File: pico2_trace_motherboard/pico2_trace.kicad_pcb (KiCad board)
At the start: 2 copper layers, 65 x 34 mm, 0 parts

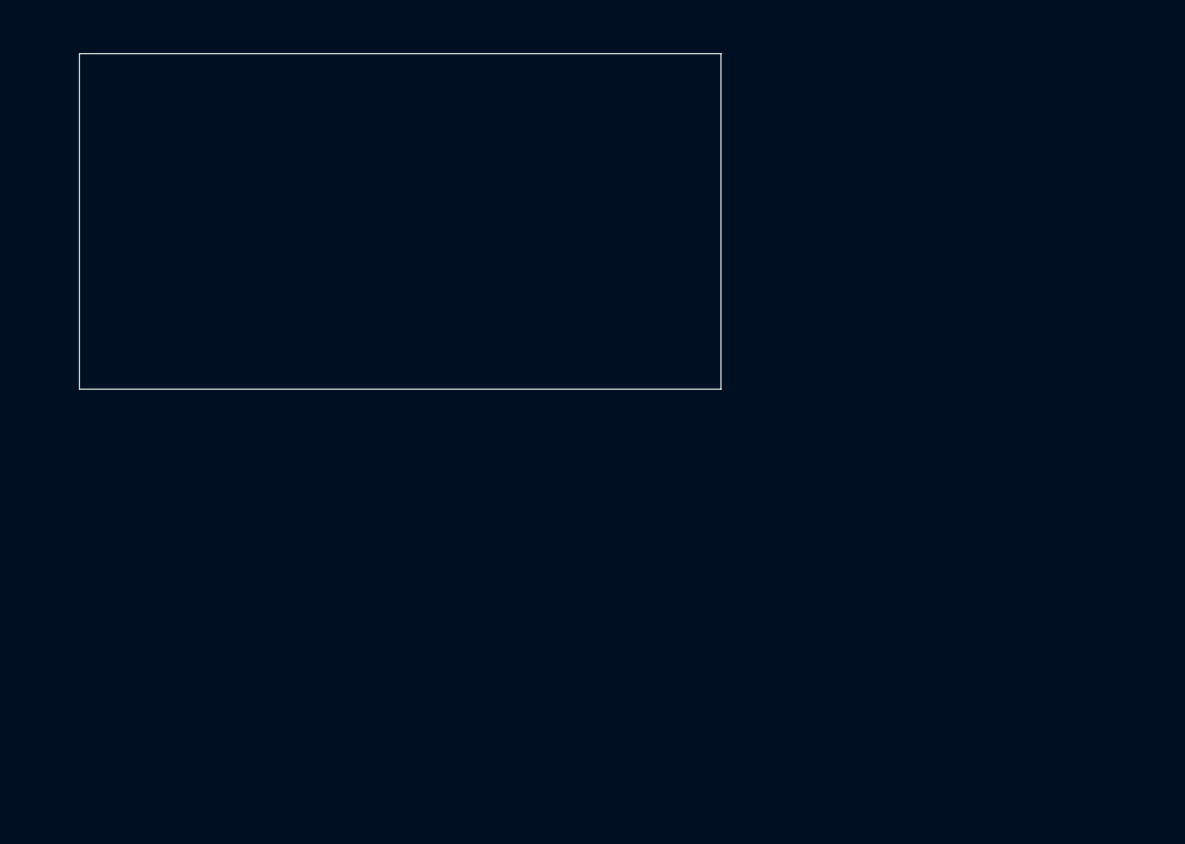
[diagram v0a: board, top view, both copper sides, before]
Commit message: pcb: footprints, nets, outline, constrained placement + trace silk
Squash of cd813c2, 6b1452c, 6e620d1.
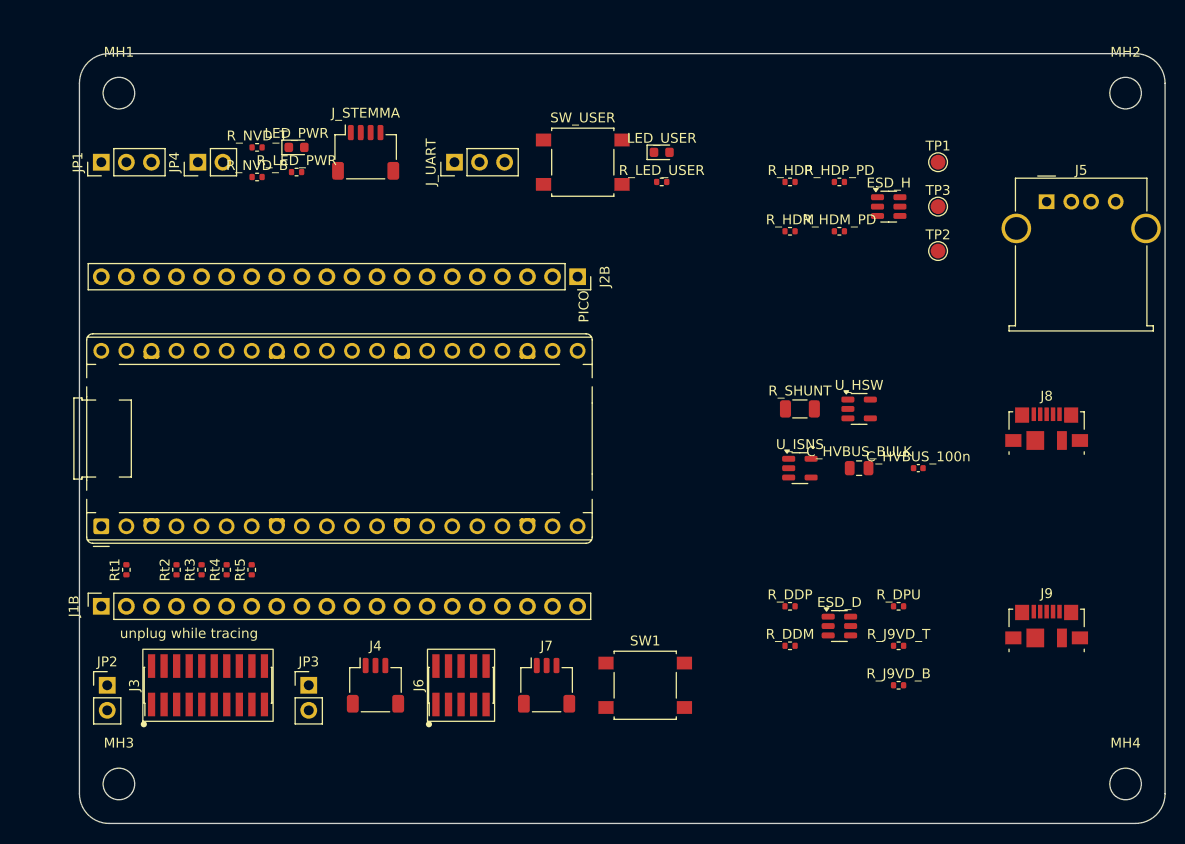
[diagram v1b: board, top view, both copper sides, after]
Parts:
- added C_HVBUS_100n: 100n, C_0402_1005Metric, F.Cu at (85.0, 42.0)
- added C_HVBUS_BULK: 22u, C_0805_2012Metric, F.Cu at (79.0, 42.0)
- added ESD_D: USBLC6-2SC6, SOT-23-6, F.Cu at (77.0, 58.0)
- added ESD_H: USBLC6-2SC6, SOT-23-6, F.Cu at (82.0, 15.5)
- added J1B: BREAKOUT, PinSocket_1x20_P2.54mm_Vertical, F.Cu at (2.21, 56.0)
- added J2B: BREAKOUT, PinSocket_1x20_P2.54mm_Vertical, F.Cu at (50.5, 22.6)
- added J3: MIPI-20, FTSH-110-01-DV, F.Cu at (13.0, 64.0)
- added J4: JST-SH-3 DEBUG, JST_SH_SM03B-SRSS-TB_1x03-1MP_P1.00mm_Horizontal, F.Cu at (30.0, 64.0)
- added J5: USB-A HOST, USB_A_Molex_67643_Horizontal, F.Cu at (98.0, 15.0)
- added J6: CORTEX-10, FTSH-105-01-DV, F.Cu at (38.7, 64.0)
- added J7: JST-SH-3 DEBUG_PROBE, JST_SH_SM03B-SRSS-TB_1x03-1MP_P1.00mm_Horizontal, F.Cu at (47.3, 64.0)
- added J8: USB-MICROB PWR, USB_Micro-B_Molex_47346-0001, F.Cu at (98.0, 38.0)
- added J9: USB-MICROB DEV, USB_Micro-B_Molex_47346-0001, F.Cu at (98.0, 58.0)
- added JP1: 5V SEL, PinHeader_1x03_P2.54mm_Vertical, F.Cu at (2.21, 11.0)
- added JP2: GP0 GUARD, PinHeader_1x02_P2.54mm_Vertical, F.Cu at (2.81, 64.0)
- added JP3: GP6 GUARD, PinHeader_1x02_P2.54mm_Vertical, F.Cu at (23.2, 64.0)
- added JP4: VBUS_DET EN, PinHeader_1x02_P2.54mm_Vertical, F.Cu at (12.0, 11.0)
- added J_STEMMA: STEMMA-QT, JST_SH_SM04B-SRSS-TB_1x04-1MP_P1.00mm_Horizontal, F.Cu at (29.0, 10.0)
- added J_UART: UART0, PinHeader_1x03_P2.54mm_Vertical, F.Cu at (38.0, 11.0)
- added LED_PWR: LED, LED_0603_1608Metric, F.Cu at (22.0, 9.50)
- added LED_USER: LED, LED_0603_1608Metric, F.Cu at (59.0, 10.0)
- added MH1: MountingHole_3.2mm_M3, MountingHole_3.2mm_M3, F.Cu at (4.00, 4.00)
- added MH2: MountingHole_3.2mm_M3, MountingHole_3.2mm_M3, F.Cu at (106.0, 4.00)
- added MH3: MountingHole_3.2mm_M3, MountingHole_3.2mm_M3, F.Cu at (4.00, 74.0)
- added MH4: MountingHole_3.2mm_M3, MountingHole_3.2mm_M3, F.Cu at (106.0, 74.0)
- added PICO: Pico2, RaspberryPi_Pico_Common_THT, F.Cu at (2.21, 47.9)
- added R_DDM: 22, R_0402_1005Metric, F.Cu at (72.0, 60.0)
- added R_DDP: 22, R_0402_1005Metric, F.Cu at (72.0, 56.0)
- added R_DPU: 1.5k, R_0402_1005Metric, F.Cu at (83.0, 56.0)
- added R_HDM: 22, R_0402_1005Metric, F.Cu at (72.0, 18.0)
- added R_HDM_PD: 15k, R_0402_1005Metric, F.Cu at (77.0, 18.0)
- added R_HDP: 22, R_0402_1005Metric, F.Cu at (72.0, 13.0)
- added R_HDP_PD: 15k, R_0402_1005Metric, F.Cu at (77.0, 13.0)
- added R_J9VD_B: 8.2k, R_0402_1005Metric, F.Cu at (83.0, 64.0)
- added R_J9VD_T: 8.2k, R_0402_1005Metric, F.Cu at (83.0, 60.0)
- added R_LED_PWR: 1k, R_0402_1005Metric, F.Cu at (22.0, 12.0)
- added R_LED_USER: 1k, R_0402_1005Metric, F.Cu at (59.0, 13.0)
- added R_NVD_B: 8.2k, R_0402_1005Metric, F.Cu at (18.0, 12.5)
- added R_NVD_T: 8.2k, R_0402_1005Metric, F.Cu at (18.0, 9.50)
- added R_SHUNT: 0.1, R_1206_3216Metric, F.Cu at (73.0, 36.0)
- added Rt1: 27, R_0402_1005Metric, F.Cu at (4.75, 52.3)
- added Rt2: 27, R_0402_1005Metric, F.Cu at (9.84, 52.3)
- added Rt3: 27, R_0402_1005Metric, F.Cu at (12.4, 52.3)
- added Rt4: 27, R_0402_1005Metric, F.Cu at (14.9, 52.3)
- added Rt5: 27, R_0402_1005Metric, F.Cu at (17.5, 52.3)
- added SW1: RESET, SW_SPST_B3S-1000, F.Cu at (57.3, 64.0)
- added SW_USER: USER, SW_SPST_B3S-1000, F.Cu at (51.0, 11.0)
- added TP1: TP, TestPoint_Pad_D1.5mm, F.Cu at (87.0, 11.0)
- added TP2: TP, TestPoint_Pad_D1.5mm, F.Cu at (87.0, 20.0)
- added TP3: TP, TestPoint_Pad_D1.5mm, F.Cu at (87.0, 15.5)
- added U_HSW: TPS2051B, SOT-23-5, F.Cu at (79.0, 36.0)
- added U_ISNS: INA180A1DBVR, SOT-23-5, F.Cu at (73.0, 42.0)
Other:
- board size 65 x 34 mm -> 110 x 78 mm
- board text added: "unplug while tracing"

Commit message: pcb: trace bundle, SWD tree, power/USB routing; DNP realization
Length-matched trace bundle; edge connectors rotated to face edges;
INA219 option, EN pulldown, cap ratings. Squash of 5ebbf61..2de5eea (4).
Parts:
- added C_NRESET: 100n/16V, C_0402_1005Metric, F.Cu at (0.00, 0.00)
- added D_J9_BUSPWR: 1N4148W, D_SOD-123, F.Cu at (0.00, 0.00)
- added J_TRACE_TP: TRACE_TP, PinHeader_1x06_P2.54mm_Vertical, F.Cu at (0.00, 0.00)
- added R_HVEN_PD: 100k, R_0402_1005Metric, F.Cu at (0.00, 0.00)
- added U_INA219_ALT: INA219, SOT-23-8, F.Cu at (0.00, 0.00)
- C_HVBUS_100n: value 100n -> 100n/16V
- C_HVBUS_BULK: value 22u -> 22u/10V
- moved ESD_D 9.17 mm to (85.3, 62.0)
- moved J8 9.17 mm to (106.3, 42.0), turned to 90 degrees
- moved J9 9.17 mm to (106.3, 62.0), turned to 90 degrees
- moved R_DDM 9.17 mm to (80.3, 64.0)
- moved R_DDP 9.17 mm to (80.3, 60.0)
- moved R_DPU 9.17 mm to (91.3, 60.0)
- moved R_J9VD_B 9.17 mm to (91.3, 68.0)
- moved R_J9VD_T 9.17 mm to (91.3, 64.0)
- moved ESD_H 6.65 mm to (80.6, 22.0)
- moved J5 6.65 mm to (96.6, 21.5), turned to 90 degrees
- moved R_HDM 6.65 mm to (70.6, 24.5)
- moved R_HDM_PD 6.65 mm to (75.6, 24.5)
- moved R_HDP 6.65 mm to (70.6, 19.5)
- moved R_HDP_PD 6.65 mm to (75.6, 19.5)
- moved TP1 6.65 mm to (85.6, 17.5)
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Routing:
- net VBUS_NET: track 0.00 -> 171.2 mm, vias 0 -> 2
- net P3V3: track 0.00 -> 129.8 mm, vias 0 -> 8
- net NRESET: track 0.00 -> 124.8 mm, vias 0 -> 9
- net VBUS_SEL: track 0.00 -> 108.3 mm, vias 0 -> 2
- net SWDIO: track 0.00 -> 71.7 mm, vias 0 -> 4
- net SWCLK: track 0.00 -> 69.2 mm, vias 0 -> 12
- net NATIVE_VBUS_DET: track 0.00 -> 61.3 mm
- net HOST_VBUS: track 0.00 -> 48.0 mm, vias 0 -> 2
- net HOST_DM: track 0.00 -> 30.7 mm
- net DEV_DP: track 0.00 -> 28.8 mm
- net HOST_DP: track 0.00 -> 28.4 mm
- net J9_VBUS: track 0.00 -> 21.1 mm
- net HOST_5V_IN: track 0.00 -> 20.4 mm
- net TD1: track 0.00 -> 19.6 mm
- net TD2: track 0.00 -> 19.2 mm
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
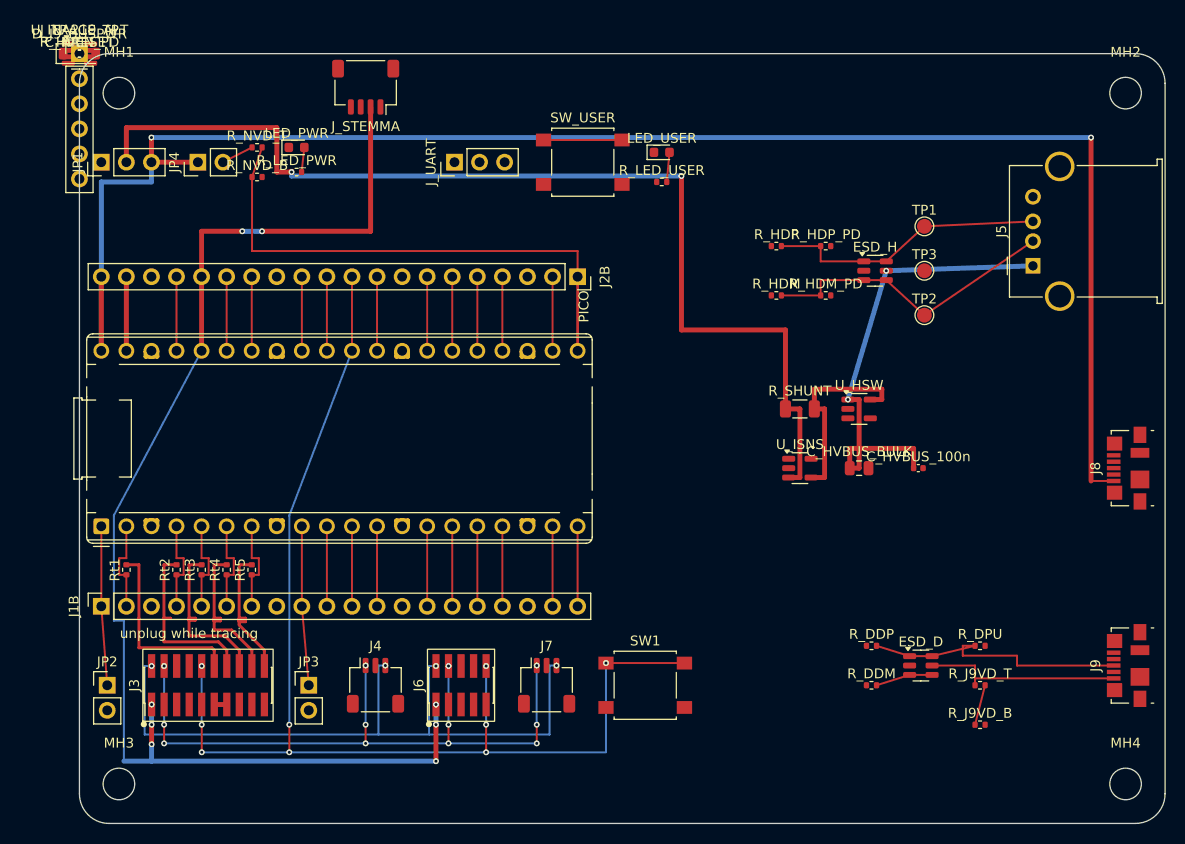
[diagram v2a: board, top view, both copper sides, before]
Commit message: pcb: compact to 92x64; SMT-socket detour reverted to THT
Co-designed placement + routing rewrite; hand-inserted connectors back
to THT after the SMD experiment. Squash of 4fb3f47..d5493a2 (5).
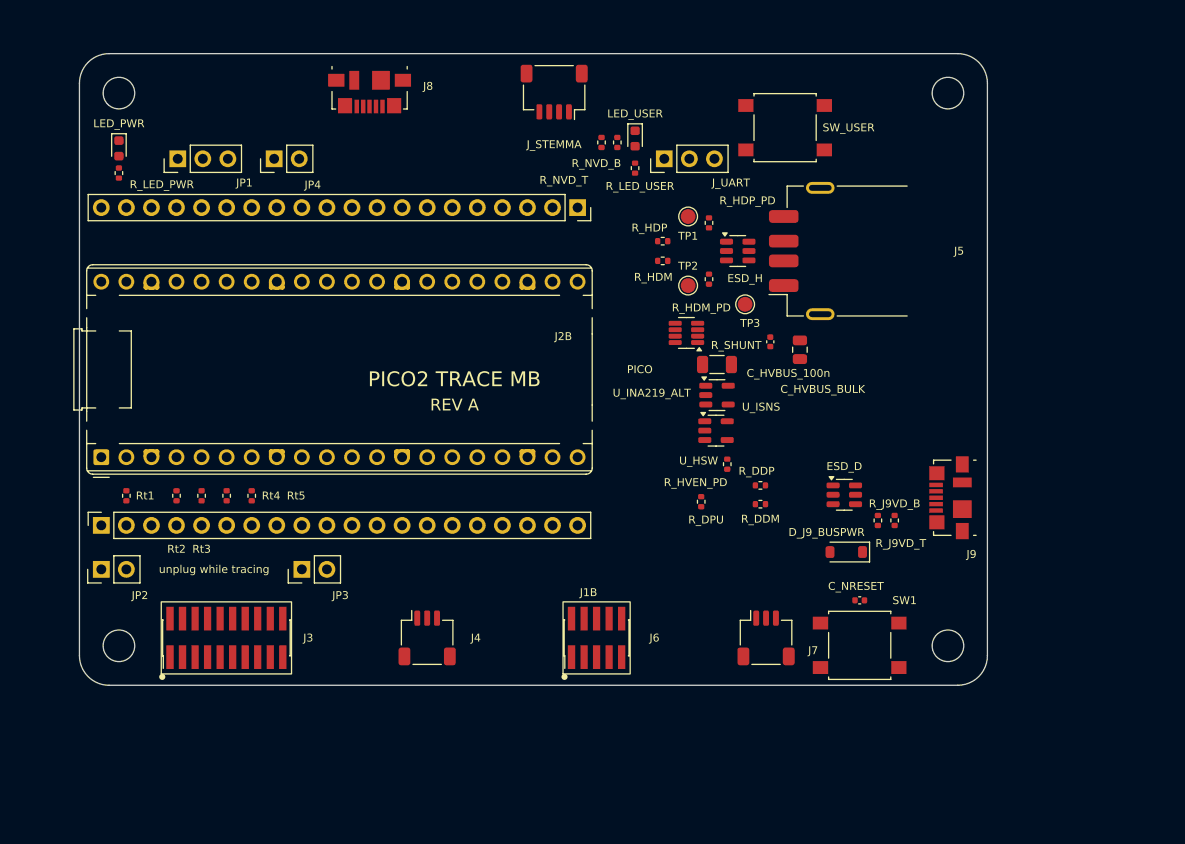
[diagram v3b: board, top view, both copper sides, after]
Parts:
- removed J_TRACE_TP: TRACE_TP, PinHeader_1x06_P2.54mm_Vertical
- J5: footprint USB_A_Molex_67643_Horizontal -> USB_A_Receptacle_GCT_USB1046
- moved C_NRESET 96.5 mm to (79.1, 55.4)
- moved D_J9_BUSPWR 92.7 mm to (77.7, 50.5), turned to 180 degrees
- moved J8 85.8 mm to (29.4, 3.90), turned to 180 degrees
- moved R_HVEN_PD 77.7 mm to (65.6, 41.6), turned to -90 degrees
- moved U_INA219_ALT 67.7 mm to (61.5, 28.3), turned to 180 degrees
- moved R_NVD_B 36.7 mm to (54.5, 9.00), turned to -90 degrees
- moved R_NVD_T 34.9 mm to (52.9, 9.00), turned to 90 degrees
- moved R_DPU 31.8 mm to (63.0, 45.4), turned to -90 degrees
- moved J9 24.8 mm to (88.3, 45.0)
- moved TP2 24.1 mm to (61.7, 23.5)
- moved TP1 24.0 mm to (61.7, 16.5)
- moved R_J9VD_B 23.1 mm to (80.9, 47.3), turned to -90 degrees
- moved MH4 22.8 mm to (88.0, 60.0)
- moved J7 22.7 mm to (69.6, 59.2)
- moved SW1 22.1 mm to (79.1, 60.0)
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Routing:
- net VBUS_NET: track 171.2 -> 0.00 mm, vias 2 -> 0
- net P3V3: track 129.8 -> 0.00 mm, vias 8 -> 0
- net NRESET: track 124.8 -> 0.00 mm, vias 9 -> 0
- net VBUS_SEL: track 108.3 -> 0.00 mm, vias 2 -> 0
- net SWDIO: track 71.7 -> 0.00 mm, vias 4 -> 0
- net SWCLK: track 69.2 -> 0.00 mm, vias 12 -> 0
- net NATIVE_VBUS_DET: track 61.3 -> 0.00 mm
- net HOST_VBUS: track 48.0 -> 0.00 mm, vias 2 -> 0
- net HOST_DM: track 30.7 -> 0.00 mm
- net DEV_DP: track 28.8 -> 0.00 mm
- net HOST_DP: track 28.4 -> 0.00 mm
- net J9_VBUS: track 21.1 -> 0.00 mm
- net HOST_5V_IN: track 20.4 -> 0.00 mm
- net TD1: track 19.6 -> 0.00 mm
- net TD2: track 19.2 -> 0.00 mm
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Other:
- board size 110 x 78 mm -> 92 x 64 mm
- board text added: "PICO2 TRACE MB"
- board text added: "REV A"

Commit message: pcb: complete routing, GND pours + stitching, power widening
All copper 0 non-GND unconnected; J10 SWD dupont added, redundant J4
removed, antenna keepout cleared; VBUS_NET widened; both-layer GND
zones + stitching vias. Squash of 0dd589d, 7224fb8, 98ee5bf, 9fa26b4.
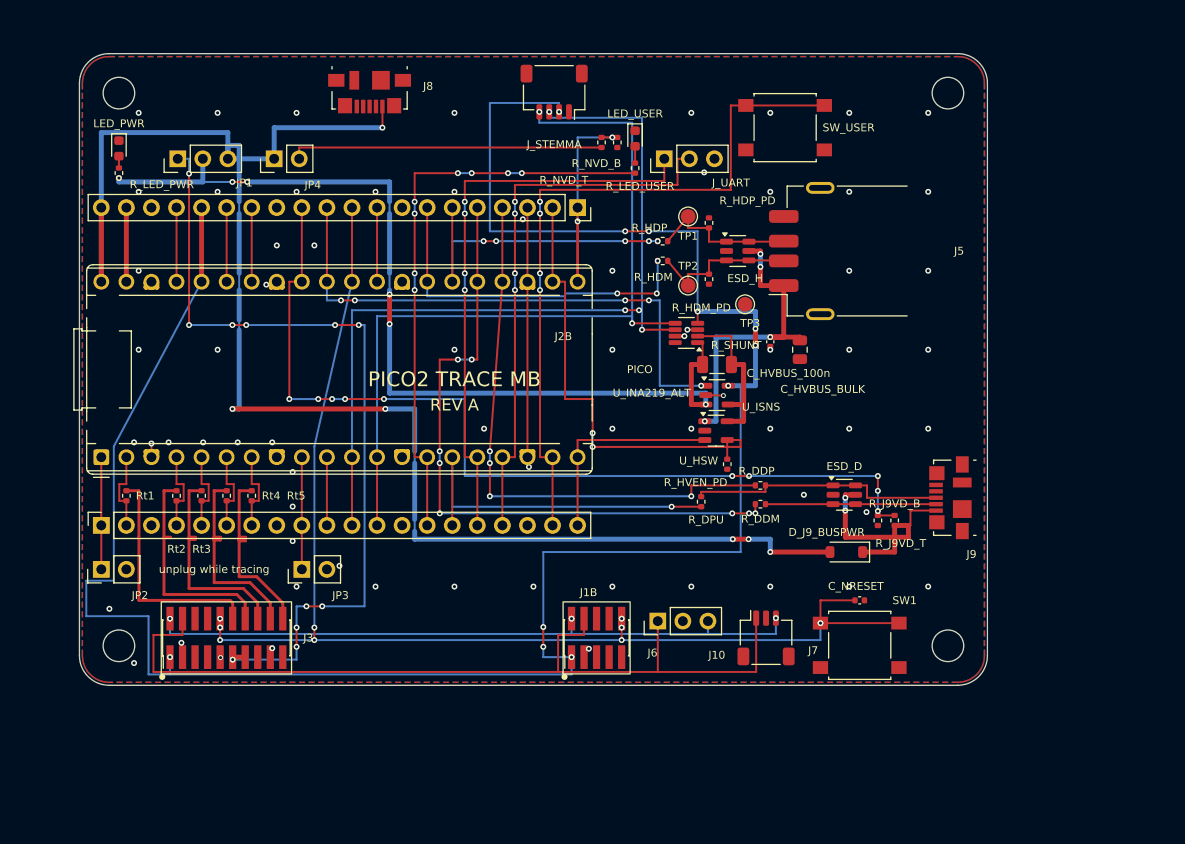
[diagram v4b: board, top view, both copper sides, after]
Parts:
- removed J4: JST-SH-3 DEBUG, JST_SH_SM03B-SRSS-TB_1x03-1MP_P1.00mm_Horizontal
- added J10: SWD, PinHeader_1x03_P2.54mm_Vertical, F.Cu at (58.6, 57.5)
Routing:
- net P3V3: track 0.00 -> 224.0 mm, vias 0 -> 11
- net VBUS_NET: track 0.00 -> 164.0 mm, vias 0 -> 6
- net NRESET: track 0.00 -> 124.9 mm, vias 0 -> 9
- net VBUS_SEL: track 0.00 -> 94.1 mm, vias 0 -> 6
- net DEV_VBUS_DET: track 0.00 -> 93.8 mm, vias 0 -> 10
- net SWCLK: track 0.00 -> 88.0 mm
- net I2C0_SDA: track 0.00 -> 88.0 mm, vias 0 -> 4
- net V5_JTRACE: track 0.00 -> 84.6 mm, vias 0 -> 11
- net I2C0_SCL: track 0.00 -> 83.0 mm, vias 0 -> 2
- net BTN_USER: track 0.00 -> 72.6 mm, vias 0 -> 4
- net GP19: track 0.00 -> 67.7 mm, vias 0 -> 8
- net SWDIO: track 0.00 -> 67.4 mm, vias 0 -> 3
- net GP10: track 0.00 -> 59.3 mm, vias 0 -> 8
- net UART0_TX: track 0.00 -> 58.6 mm, vias 0 -> 4
- net GP18: track 0.00 -> 57.3 mm, vias 0 -> 4
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- added copper zone on B.Cu, net GND
- added copper zone on F.Cu, net GND
